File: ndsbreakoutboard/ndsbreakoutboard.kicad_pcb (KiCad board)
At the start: 2 copper layers, 27.3 x 30.5 mm, 17 parts, among them U1 ndsPADS

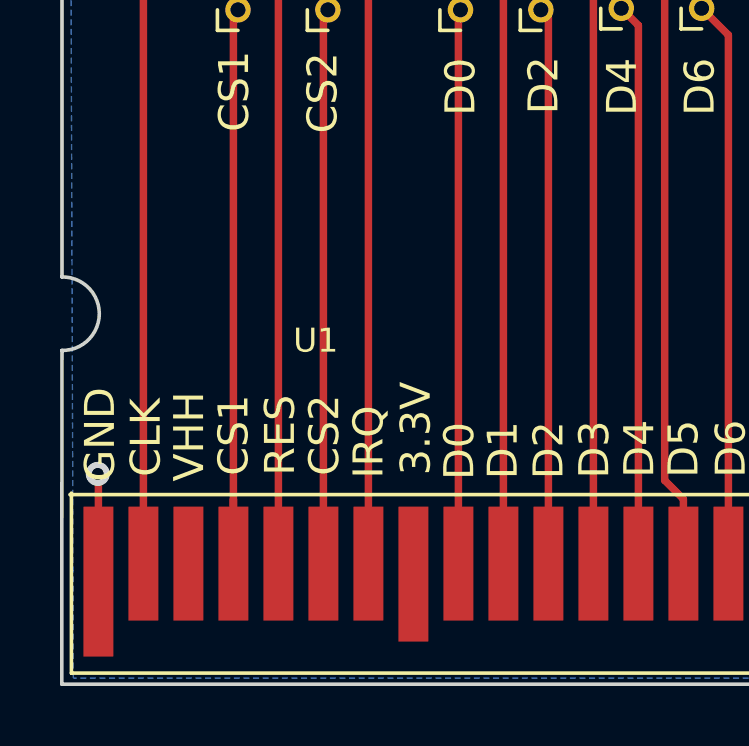
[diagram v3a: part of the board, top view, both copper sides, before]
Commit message: Minor fixes
Schematic modified again, adding the mising unused pins and reflected in PCB
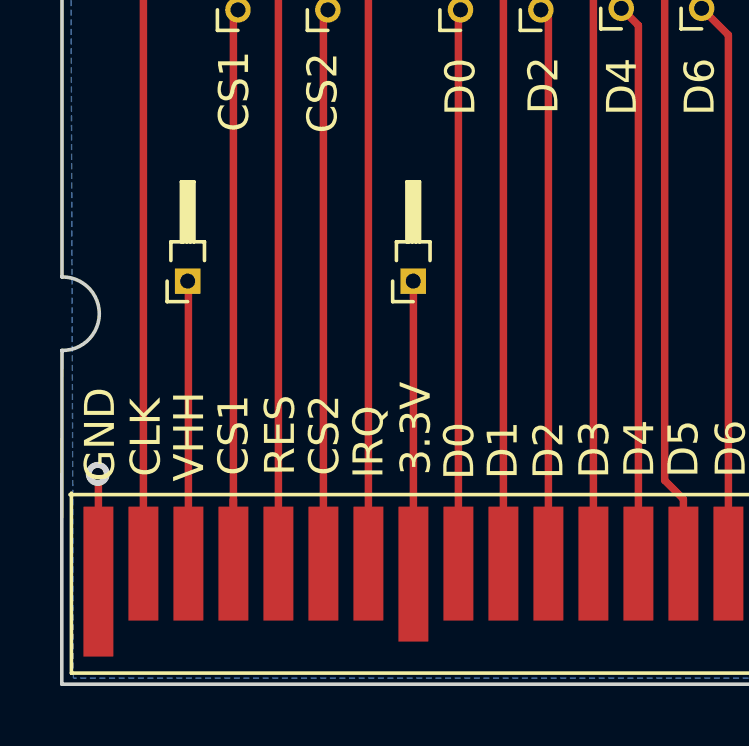
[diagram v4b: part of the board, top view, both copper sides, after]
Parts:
- added 3.3V: Conn_01x01_Female, Connector_PinHeader_1.00mm:PinHeader_1x01_P1.00mm_Horizontal, F.Cu at (96.2, 78.6)
- added J14: Conn_01x01_Female, Connector_PinHeader_1.00mm:PinHeader_1x01_P1.00mm_Horizontal, F.Cu at (88.6, 78.6)
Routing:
- net Net-(J15-Pad1): track 0.00 -> 9.78 mm
- net Net-(J14-Pad1): track 0.00 -> 9.43 mm
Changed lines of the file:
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@@
     (thickness 1.6)
     (drawings 27)
-    (tracks 41)
+    (tracks 46)
     (zones 0)
-    (modules 17)
+    (modules 19)
     (nets 17)
   )
@@
   (net 13 "Net-(J12-Pad1)")
   (net 14 "Net-(J13-Pad1)")
-  (net 15 "Net-(U1-Pad3)")
-  (net 16 "Net-(U1-Pad8)")
+  (net 15 "Net-(J14-Pad1)")
+  (net 16 "Net-(J15-Pad1)")
   (net_class Default "Esta es la clase de red por defecto."
     (clearance 0.1999)
@@
     (add_net "Net-(J12-Pad1)")
     (add_net "Net-(J13-Pad1)")
+    (add_net "Net-(J14-Pad1)")
+    (add_net "Net-(J15-Pad1)")
     (add_net "Net-(J2-Pad1)")
     (add_net "Net-(J3-Pad1)")
@@
     (add_net "Net-(J8-Pad1)")
     (add_net "Net-(J9-Pad1)")
-    (add_net "Net-(U1-Pad3)")
-    (add_net "Net-(U1-Pad8)")
   )
   (module Connector:ndsIcon (layer F.Cu)
@@
     (descr "A footprint for the bottom pads of the NDS cartridge")
     (tags "nds nintendo ds 3ds dsi pads bottom cart card")
-    (fp_text reference U1 (at 0.143199 -4.0854) (layer F.SilkS)
+    (fp_text reference U1 (at 0.143199 -4.0854) (layer F.SilkS) hide
       (effects (font (size 0.8 0.8) (thickness 0.15)))
     )
@@
       (net 3 "Net-(J2-Pad1)"))
     (pad 3 smd rect (at -4.1 3.35) (size 1 3.8) (layers F.Cu F.Paste F.Mask)
-      (net 15 "Net-(U1-Pad3)"))
+      (net 15 "Net-(J14-Pad1)"))
     (pad 7 smd rect (at 1.9 3.35) (size 1 3.8) (layers F.Cu F.Paste F.Mask)
       (net 6 "Net-(J5-Pad1)"))
@@
       (net 4 "Net-(J3-Pad1)"))
     (pad 8 smd rect (at 3.4 3.7) (size 1 4.5) (layers F.Cu F.Paste F.Mask)
-      (net 16 "Net-(U1-Pad8)"))
+      (net 16 "Net-(J15-Pad1)"))
     (pad 11 smd rect (at 7.9 3.35) (size 1 3.8) (layers F.Cu F.Paste F.Mask)
       (net 9 "Net-(J8-Pad1)"))
@@
     (pad 1 thru_hole circle (at 0 0 90) (size 0.85 0.85) (drill 0.5) (layers *.Cu *.Mask)
       (net 14 "Net-(J13-Pad1)"))
+    (model ${KISYS3DMOD}/Connector_PinHeader_1.00mm.3dshapes/PinHeader_1x01_P1.00mm_Horizontal.wrl
+      (at (xyz 0 0 0))
+      (scale (xyz 1 1 1))
+      (rotate (xyz 0 0 0))
+    )
+  )
+  (module Connector_PinHeader_1.00mm:PinHeader_1x01_P1.00mm_Horizontal (layer F.Cu)
+    (at 88.646 78.6384 90)
+    (descr "Through hole angled pin header, 1x01, 1.00mm pitch, 2.0mm pin length, single row")
+    (tags "Through hole angled pin header THT 1x01 1.00mm single row")
+    (fp_text reference J14 (at 1.375 -1.5 90) (layer F.SilkS) hide
+      (effects (font (size 1 1) (thickness 0.15)))
+    )
+    (fp_text value Conn_01x01_Female (at 1.375 1.5 90) (layer F.Fab)
+      (effects (font (size 1 1) (thickness 0.15)))
+    )
+    (fp_line (start 0.5 -0.5) (end 1.25 -0.5) (layer F.Fab) (width 0.1))
+    (fp_line (start 1.25 -0.5) (end 1.25 0.5) (layer F.Fab) (width 0.1))
+    (fp_line (start 1.25 0.5) (end 0.25 0.5) (layer F.Fab) (width 0.1))
+    (fp_line (start 0.25 0.5) (end 0.25 -0.25) (layer F.Fab) (width 0.1))
+    (fp_line (start 0.25 -0.25) (end 0.5 -0.5) (layer F.Fab) (width 0.1))
+    (fp_line (start -0.15 -0.15) (end 0.25 -0.15) (layer F.Fab) (width 0.1))
+    (fp_line (start -0.15 -0.15) (end -0.15 0.15) (layer F.Fab) (width 0.1))
+    (fp_line (start -0.15 0.15) (end 0.25 0.15) (layer F.Fab) (width 0.1))
+    (fp_line (start 1.25 -0.15) (end 3.25 -0.15) (layer F.Fab) (width 0.1))
+    (fp_line (start 3.25 -0.15) (end 3.25 0.15) (layer F.Fab) (width 0.1))
+    (fp_line (start 1.25 0.15) (end 3.25 0.15) (layer F.Fab) (width 0.1))
+    (fp_line (start 0.685 -0.56) (end 1.31 -0.56) (layer F.SilkS) (width 0.12))
+    (fp_line (start 1.31 -0.56) (end 1.31 0.56) (layer F.SilkS) (width 0.12))
+    (fp_line (start 1.31 0.56) (end 0.685 0.56) (layer F.SilkS) (width 0.12))
+    (fp_line (start 1.31 -0.21) (end 3.31 -0.21) (layer F.SilkS) (width 0.12))
+    (fp_line (start 3.31 -0.21) (end 3.31 0.21) (layer F.SilkS) (width 0.12))
+    (fp_line (start 3.31 0.21) (end 1.31 0.21) (layer F.SilkS) (width 0.12))
+    (fp_line (start 1.31 -0.15) (end 3.31 -0.15) (layer F.SilkS) (width 0.12))
+    (fp_line (start 1.31 -0.03) (end 3.31 -0.03) (layer F.SilkS) (width 0.12))
+    (fp_line (start 1.31 0.09) (end 3.31 0.09) (layer F.SilkS) (width 0.12))
+    (fp_line (start -0.685 0) (end -0.685 -0.685) (layer F.SilkS) (width 0.12))
+    (fp_line (start -0.685 -0.685) (end 0 -0.685) (layer F.SilkS) (width 0.12))
+    (fp_line (start -1 -1) (end -1 1) (layer F.CrtYd) (width 0.05))
+    (fp_line (start -1 1) (end 3.75 1) (layer F.CrtYd) (width 0.05))
+    (fp_line (start 3.75 1) (end 3.75 -1) (layer F.CrtYd) (width 0.05))
+    (fp_line (start 3.75 -1) (end -1 -1) (layer F.CrtYd) (width 0.05))
+    (fp_text user %R (at 0.75 0) (layer F.Fab)
+      (effects (font (size 0.6 0.6) (thickness 0.09)))
+    )
+    (pad 1 thru_hole rect (at 0 0 90) (size 0.85 0.85) (drill 0.5) (layers *.Cu *.Mask)
+      (net 15 "Net-(J14-Pad1)"))
+    (model ${KISYS3DMOD}/Connector_PinHeader_1.00mm.3dshapes/PinHeader_1x01_P1.00mm_Horizontal.wrl
+      (at (xyz 0 0 0))
+      (scale (xyz 1 1 1))
+      (rotate (xyz 0 0 0))
+    )
+  )
+  (module Connector_PinHeader_1.00mm:PinHeader_1x01_P1.00mm_Horizontal (layer F.Cu)
+    (at 96.1644 78.6384 90)
+    (descr "Through hole angled pin header, 1x01, 1.00mm pitch, 2.0mm pin length, single row")
+    (tags "Through hole angled pin header THT 1x01 1.00mm single row")
+    (fp_text reference 3.3V (at -2.5908 0 90) (layer F.SilkS) hide
+      (effects (font (size 1 1) (thickness 0.15)))
+    )
+    (fp_text value Conn_01x01_Female (at 1.375 1.5 90) (layer F.Fab)
+      (effects (font (size 1 1) (thickness 0.15)))
+    )
+    (fp_line (start 0.5 -0.5) (end 1.25 -0.5) (layer F.Fab) (width 0.1))
+    (fp_line (start 1.25 -0.5) (end 1.25 0.5) (layer F.Fab) (width 0.1))
+    (fp_line (start 1.25 0.5) (end 0.25 0.5) (layer F.Fab) (width 0.1))
+    (fp_line (start 0.25 0.5) (end 0.25 -0.25) (layer F.Fab) (width 0.1))
+    (fp_line (start 0.25 -0.25) (end 0.5 -0.5) (layer F.Fab) (width 0.1))
+    (fp_line (start -0.15 -0.15) (end 0.25 -0.15) (layer F.Fab) (width 0.1))
+    (fp_line (start -0.15 -0.15) (end -0.15 0.15) (layer F.Fab) (width 0.1))
+    (fp_line (start -0.15 0.15) (end 0.25 0.15) (layer F.Fab) (width 0.1))
+    (fp_line (start 1.25 -0.15) (end 3.25 -0.15) (layer F.Fab) (width 0.1))
+    (fp_line (start 3.25 -0.15) (end 3.25 0.15) (layer F.Fab) (width 0.1))
+    (fp_line (start 1.25 0.15) (end 3.25 0.15) (layer F.Fab) (width 0.1))
+    (fp_line (start 0.685 -0.56) (end 1.31 -0.56) (layer F.SilkS) (width 0.12))
+    (fp_line (start 1.31 -0.56) (end 1.31 0.56) (layer F.SilkS) (width 0.12))
+    (fp_line (start 1.31 0.56) (end 0.685 0.56) (layer F.SilkS) (width 0.12))
+    (fp_line (start 1.31 -0.21) (end 3.31 -0.21) (layer F.SilkS) (width 0.12))
+    (fp_line (start 3.31 -0.21) (end 3.31 0.21) (layer F.SilkS) (width 0.12))
+    (fp_line (start 3.31 0.21) (end 1.31 0.21) (layer F.SilkS) (width 0.12))
+    (fp_line (start 1.31 -0.15) (end 3.31 -0.15) (layer F.SilkS) (width 0.12))
+    (fp_line (start 1.31 -0.03) (end 3.31 -0.03) (layer F.SilkS) (width 0.12))
+    (fp_line (start 1.31 0.09) (end 3.31 0.09) (layer F.SilkS) (width 0.12))
+    (fp_line (start -0.685 0) (end -0.685 -0.685) (layer F.SilkS) (width 0.12))
+    (fp_line (start -0.685 -0.685) (end 0 -0.685) (layer F.SilkS) (width 0.12))
+    (fp_line (start -1 -1) (end -1 1) (layer F.CrtYd) (width 0.05))
+    (fp_line (start -1 1) (end 3.75 1) (layer F.CrtYd) (width 0.05))
+    (fp_line (start 3.75 1) (end 3.75 -1) (layer F.CrtYd) (width 0.05))
+    (fp_line (start 3.75 -1) (end -1 -1) (layer F.CrtYd) (width 0.05))
+    (fp_text user %R (at 0.75 0) (layer F.Fab)
+      (effects (font (size 0.6 0.6) (thickness 0.09)))
+    )
+    (pad 1 thru_hole rect (at 0 0 90) (size 0.85 0.85) (drill 0.5) (layers *.Cu *.Mask)
+      (net 16 "Net-(J15-Pad1)"))
     (model ${KISYS3DMOD}/Connector_PinHeader_1.00mm.3dshapes/PinHeader_1x01_P1.00mm_Horizontal.wrl
       (at (xyz 0 0 0))
@@
   (segment (start 108.170001 69.833199) (end 108.458 69.5452) (width 0.25) (layer F.Cu) (net 14))
   (segment (start 108.170001 88.055) (end 108.170001 69.833199) (width 0.25) (layer F.Cu) (net 14))
+  (segment (start 88.670001 78.662401) (end 88.646 78.6384) (width 0.25) (layer F.Cu) (net 15))
+  (segment (start 88.670001 88.055) (end 88.670001 78.662401) (width 0.25) (layer F.Cu) (net 15))
+  (segment (start 96.170001 76.942201) (end 96.1644 76.9366) (width 0.25) (layer F.Cu) (net 16))
+  (segment (start 96.170001 78.644001) (end 96.1644 78.6384) (width 0.25) (layer F.Cu) (net 16))
+  (segment (start 96.170001 88.405) (end 96.170001 78.644001) (width 0.25) (layer F.Cu) (net 16))
   (zone (net 1) (net_name "Net-(GNDLine1-Pad1)") (layer B.Cu) (hatch edge 0.508)
     (connect_pads (clearance 0.508))

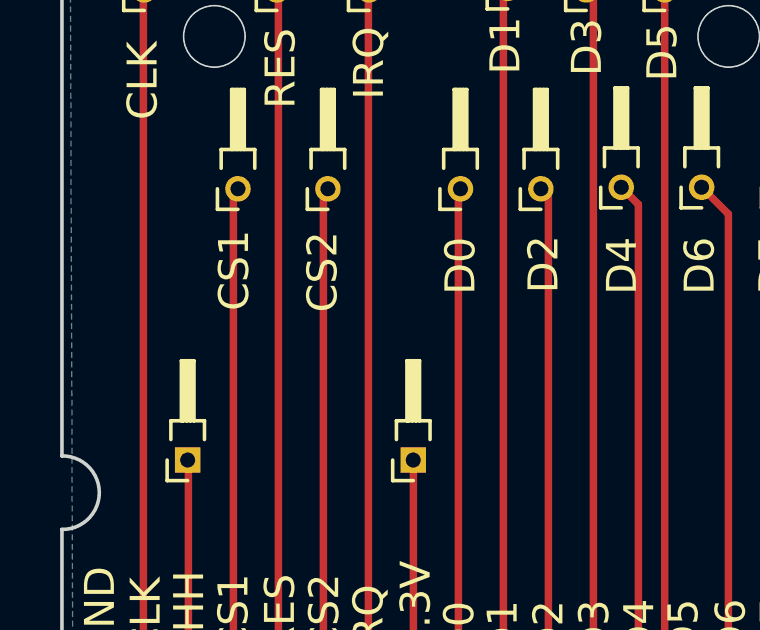
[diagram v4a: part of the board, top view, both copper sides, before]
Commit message: Release commit
Fixes the missaligned top holes
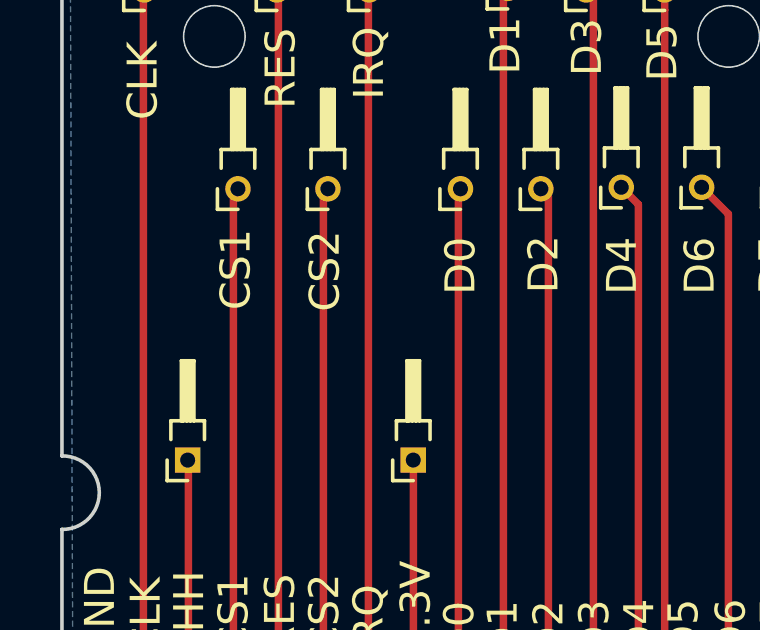
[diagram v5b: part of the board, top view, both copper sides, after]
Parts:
- moved G*** 0.20 mm to (103.5, 86.0)
- moved G*** 0.08 mm to (92.3, 86.1)
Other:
- board text added: "JLCJLCJLCJLC"

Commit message: Gerber and drill files and v1.1 updates
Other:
- board text added: "v1.1"
- board text removed: "v1.0"
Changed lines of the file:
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@@
     (41 Cmts.User user hide)
     (42 Eco1.User user hide)
-    (43 Eco2.User user)
+    (43 Eco2.User user hide)
     (44 Edge.Cuts user)
     (45 Margin user hide)
-    (46 B.CrtYd user)
+    (46 B.CrtYd user hide)
     (47 F.CrtYd user hide)
     (48 B.Fab user hide)
@@
     (effects (font (size 0.9 0.9) (thickness 0.15)) (justify mirror))
   )
-  (gr_text v1.0 (at 97.8662 85.9536) (layer B.SilkS)
+  (gr_text v1.1 (at 97.8662 85.9536) (layer B.SilkS)
     (effects (font (size 1.5 1.5) (thickness 0.3)) (justify mirror))
   )
